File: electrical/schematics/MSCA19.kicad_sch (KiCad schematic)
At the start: 0 parts

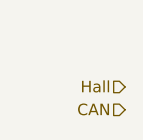
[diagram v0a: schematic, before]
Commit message: Esquematico revisado, agora mais limpo.
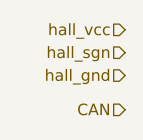
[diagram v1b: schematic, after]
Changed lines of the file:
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@@
     (effects (font (size 1.27 1.27)) (justify right))
   )
-  (hierarchical_label "Hall" (shape input) (at 27.94 31.75 180)
+  (hierarchical_label "hall_gnd" (shape input) (at 27.94 30.48 180)
     (effects (font (size 1.27 1.27)) (justify right))
   )
+  (hierarchical_label "hall_vcc" (shape input) (at 27.94 25.4 180)
+    (effects (font (size 1.27 1.27)) (justify right))
+  )
+  (hierarchical_label "hall_sgn" (shape input) (at 27.94 27.94 180)
+    (effects (font (size 1.27 1.27)) (justify right))
+  )
